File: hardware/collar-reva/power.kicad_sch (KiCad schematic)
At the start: 12 parts, among them J1 USB-C, J2 JST-PH LiPo, U2 MCP73831, U3 AP2112K-3.3

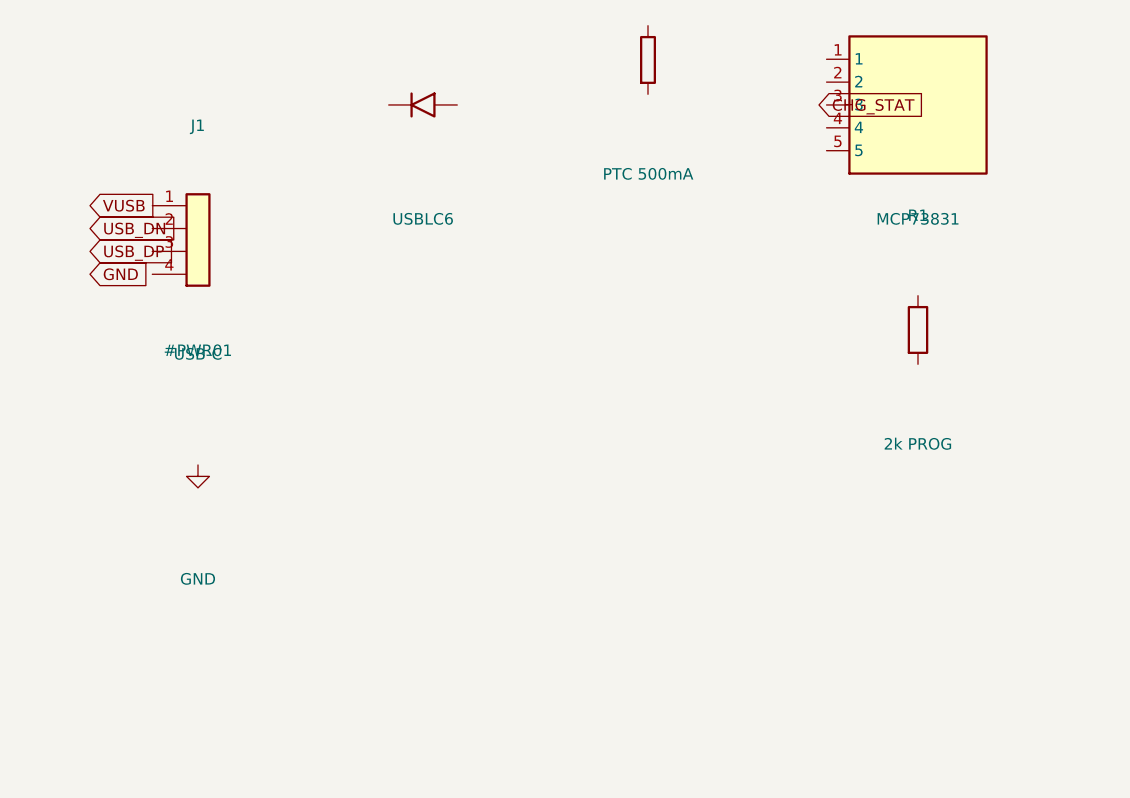
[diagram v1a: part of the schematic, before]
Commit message: feat(hw): put photodiode, USB-C CC, and footprints on the Rev-A sheets
A C-to-C cable and neck PPG both need those parts on the schematic, not as layout notes. Footprints match the BOM so layout can start; copper is still the 30 mm outline.

Co-authored-by: Cursor <cursoragent@cursor.com>
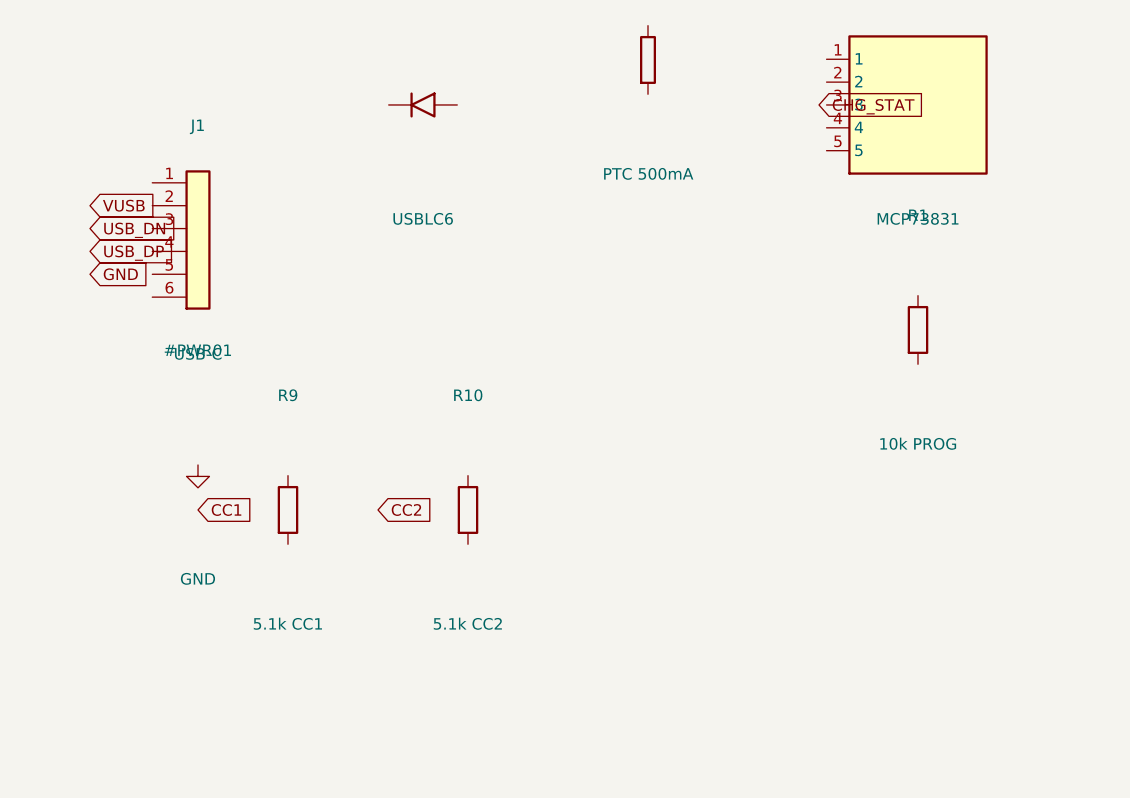
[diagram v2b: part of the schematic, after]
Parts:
- removed J1: USB-C, symbol Connector:Conn_01x04
- added J1: USB-C, Connector_USB:USB_C_Receptacle_USB4105-xx-A_16P_TopMnt_Horizontal, symbol Connector:Conn_01x06
- added R10: 5.1k CC2, Resistor_SMD:R_0402_1005Metric, symbol Device:R
- added R9: 5.1k CC1, Resistor_SMD:R_0402_1005Metric, symbol Device:R
- C1, C2: footprint (none) -> Capacitor_SMD:C_0805_2012Metric
- C3: footprint (none) -> Capacitor_SMD:C_0402_1005Metric
- D1: footprint (none) -> Package_TO_SOT_SMD:SOT-23-6
- F1: footprint (none) -> Fuse:Fuse_1812_4532Metric
- J2: footprint (none) -> Connector_JST:JST_PH_S2B-PH-SM4-TB_1x02-1MP_P2.00mm_Horizontal
- R1: value 2k PROG -> 10k PROG; footprint (none) -> Resistor_SMD:R_0402_1005Metric
- R2, R3: footprint (none) -> Resistor_SMD:R_0402_1005Metric
- U2, U3: footprint (none) -> Package_TO_SOT_SMD:SOT-23-5
